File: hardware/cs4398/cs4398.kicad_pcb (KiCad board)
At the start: 4 copper layers, 55 parts, among them J1 USB_C_Receptacle_USB2.0_16P, Q1 Si2323DS, U2 STM32H750IBKx, U3 TPS65131RGE, U4 USB3300-EZK, U5 TPS7A8300, U7 TPS60151DRV, Y1 CSTCE12M

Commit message: sync 9.15
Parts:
- removed the C13 at (133.1, 89.9)
- removed the C31 at (138.9, 93.8)
- removed the R5 at (190.7, 146.4)
- added C1: 10u, Capacitor_SMD:C_0805_2012Metric, F.Cu at (191.2, 116.2)
- added C16: 100n, Capacitor_SMD:C_0402_1005Metric, B.Cu at (195.4, 108.0)
- added C18: 100n, Capacitor_SMD:C_0402_1005Metric, B.Cu at (192.2, 108.0)
- added C19: 100u, Capacitor_Tantalum_SMD:CP_EIA-3528-15_AVX-H, F.Cu at (198.2, 105.2)
- added C20: 10u, Capacitor_SMD:C_0805_2012Metric, F.Cu at (191.0, 105.8)
- added C21: 100n, Capacitor_SMD:C_0402_1005Metric, B.Cu at (196.8, 108.0)
- added C22: 4.7u, Capacitor_SMD:C_0805_2012Metric, B.Cu at (202.8, 148.8)
- added C23: 33u, Capacitor_Tantalum_SMD:CP_EIA-3528-15_AVX-H, F.Cu at (199.6, 111.0)
- added C35: 100n, Capacitor_SMD:C_0603_1608Metric, F.Cu at (193.6, 144.1)
- added C4: 33u, Capacitor_Tantalum_SMD:CP_EIA-3528-15_AVX-H, F.Cu at (198.2, 116.7)
- added C41: 100n, Capacitor_SMD:C_0603_1608Metric, B.Cu at (181.0, 131.6)
- added C44: 6800p, Capacitor_SMD:C_0402_1005Metric, F.Cu at (144.8, 143.3)
- added C45: 6800p, Capacitor_SMD:C_0402_1005Metric, F.Cu at (147.6, 137.3)
- added C46: 100n, Capacitor_SMD:C_0402_1005Metric, B.Cu at (194.2, 123.3)
- added C47: 100n, Capacitor_SMD:C_0402_1005Metric, B.Cu at (192.2, 123.8)
- added C48: 18n, Capacitor_SMD:C_0402_1005Metric, F.Cu at (144.8, 137.3)
- added C49: 18n, Capacitor_SMD:C_0402_1005Metric, F.Cu at (147.6, 139.3)
- added C51: 100n, Capacitor_SMD:C_0402_1005Metric, B.Cu at (196.4, 123.8)
- added C52: 100n, Capacitor_SMD:C_0402_1005Metric, B.Cu at (192.6, 126.1)
- added C53: 100u, Capacitor_Tantalum_SMD:CP_EIA-3528-15_AVX-H, F.Cu at (137.5, 131.3)
- added C54: 100u, Capacitor_Tantalum_SMD:CP_EIA-3528-15_AVX-H, F.Cu at (131.1, 144.9)
- added C55: 100n, Capacitor_SMD:C_0402_1005Metric, B.Cu at (192.6, 127.2)
- added C56: 100n, Capacitor_SMD:C_0402_1005Metric, B.Cu at (199.3, 126.5)
- added C57: 4700p, Capacitor_SMD:C_0402_1005Metric, F.Cu at (147.6, 135.4)
- added C58: 4700p, Capacitor_SMD:C_0402_1005Metric, F.Cu at (147.6, 141.3)
- added C59: 100n, Capacitor_SMD:C_0402_1005Metric, B.Cu at (199.3, 127.6)
- added C6: 100n, Capacitor_SMD:C_0402_1005Metric, B.Cu at (188.9, 108.0)
- added C60: 100n, Capacitor_SMD:C_0402_1005Metric, B.Cu at (199.4, 128.7)
- added C61: 100n, Capacitor_SMD:C_0603_1608Metric, B.Cu at (207.9, 129.8)
- added C62: 100n, Capacitor_SMD:C_0603_1608Metric, F.Cu at (136.4, 143.7)
- added C62: 1800p, Capacitor_SMD:C_0805_2012Metric, F.Cu at (132.2, 128.0)
- added C63: 1800p, Capacitor_SMD:C_0805_2012Metric, F.Cu at (132.2, 137.0)
- added C64: 100n, Capacitor_SMD:C_0402_1005Metric, B.Cu at (195.3, 123.3)
- added C65: 100n, Capacitor_SMD:C_0402_1005Metric, B.Cu at (191.2, 128.9)
- added C66: 100n, Capacitor_SMD:C_0402_1005Metric, B.Cu at (193.2, 123.3)
- added C67: 100n, Capacitor_SMD:C_0402_1005Metric, B.Cu at (196.7, 132.0)
- added C68: 100n, Capacitor_SMD:C_0402_1005Metric, F.Cu at (144.8, 139.3)
- added C69: 22u, Capacitor_Tantalum_SMD:CP_EIA-3528-15_AVX-H, F.Cu at (137.5, 135.7)
- added C7: 100n, Capacitor_SMD:C_0402_1005Metric, B.Cu at (196.8, 113.9)
- added C70: 22u, Capacitor_Tantalum_SMD:CP_EIA-3528-15_AVX-H, F.Cu at (131.1, 140.6)
- added C71: 100n, Capacitor_SMD:C_0402_1005Metric, B.Cu at (189.3, 131.3)
- added C72: 100n, Capacitor_SMD:C_0402_1005Metric, B.Cu at (189.3, 132.3)
- added C73: 100u, Capacitor_SMD:C_0805_2012Metric, F.Cu at (132.2, 131.0)
- added C73: 100n, Capacitor_SMD:C_0402_1005Metric, B.Cu at (194.5, 132.0)
- added C74: 100n, Capacitor_SMD:C_0402_1005Metric, B.Cu at (195.6, 132.0)
- added C75: 22u, Capacitor_SMD:C_0805_2012Metric, F.Cu at (132.2, 134.0)
- added C75: 100n, Capacitor_SMD:C_0603_1608Metric, B.Cu at (207.9, 124.2)
- added C76: 100n, Capacitor_SMD:C_0603_1608Metric, B.Cu at (180.9, 122.4)
- added C77: 100n, Capacitor_SMD:C_0402_1005Metric, B.Cu at (191.1, 123.8)
- added C78: 100n, Capacitor_SMD:C_0402_1005Metric, B.Cu at (197.9, 129.4)
- added C79: 100n, Capacitor_SMD:C_0402_1005Metric, F.Cu at (144.8, 141.3)
- added C8: 100n, Capacitor_SMD:C_0402_1005Metric, B.Cu at (192.2, 113.9)
- added C80: 2.2u, Capacitor_SMD:C_0402_1005Metric, B.Cu at (198.1, 125.0)
- added C81: 2.2u, Capacitor_SMD:C_0402_1005Metric, B.Cu at (196.8, 129.7)
- added F1: 1A, Fuse:Fuse_0603_1608Metric, B.Cu at (207.2, 109.7)
- added J2: GH1.25-4P, Connector_JST:JST_GH_BM04B-GHS-TBT_1x04-1MP_P1.25mm_Vertical, F.Cu at (207.7, 111.6)
- added Q2: S9012, Package_TO_SOT_SMD:SOT-23, F.Cu at (127.5, 122.9)
- added Q3: S9012, Package_TO_SOT_SMD:SOT-23, F.Cu at (127.5, 127.5)
- added Q4: S9013, Package_TO_SOT_SMD:SOT-23, F.Cu at (127.5, 132.1)
- added Q5: S9013, Package_TO_SOT_SMD:SOT-23, F.Cu at (127.5, 136.7)
- added R1: 10K, Resistor_SMD:R_0402_1005Metric, B.Cu at (195.7, 113.9)
- added R10: 2k, Resistor_SMD:R_0402_1005Metric, F.Cu at (150.6, 123.4)
- added R12: 10K, Resistor_SMD:R_0402_1005Metric, F.Cu at (150.6, 125.4)
- added R13: 10K, Resistor_SMD:R_0402_1005Metric, F.Cu at (147.7, 129.4)
- added R13: 10k, Resistor_SMD:R_0603_1608Metric, F.Cu at (136.4, 146.2)
- added R14: 10K, Resistor_SMD:R_0402_1005Metric, F.Cu at (150.6, 127.4)
- added R15: 1.5K, Resistor_SMD:R_0402_1005Metric, F.Cu at (147.7, 131.4)
- added R16: 1.5K, Resistor_SMD:R_0402_1005Metric, F.Cu at (150.6, 129.4)
- added R20: 10k, Resistor_SMD:R_0603_1608Metric, F.Cu at (195.2, 144.1)
- added R22: 10k, Resistor_SMD:R_0603_1608Metric, B.Cu at (181.0, 129.8)
- added R23: 1.6k, Resistor_SMD:R_0402_1005Metric, F.Cu at (141.9, 121.5)
- added R24: 620, Resistor_SMD:R_0402_1005Metric, F.Cu at (141.9, 127.4)
- added R25: 1.6k, Resistor_SMD:R_0402_1005Metric, F.Cu at (144.8, 123.4)
- added R26: 620, Resistor_SMD:R_0402_1005Metric, F.Cu at (144.8, 125.4)
- added R27: 270, Resistor_SMD:R_0402_1005Metric, F.Cu at (141.9, 129.4)
- added R28: 270, Resistor_SMD:R_0402_1005Metric, F.Cu at (144.8, 127.4)
- added R29: 680, Resistor_SMD:R_0402_1005Metric, F.Cu at (141.9, 123.4)
- added R30: 270, Resistor_SMD:R_0402_1005Metric, F.Cu at (141.9, 125.4)
- added R31: 680, Resistor_SMD:R_0402_1005Metric, F.Cu at (144.8, 129.4)
- added R32: 270, Resistor_SMD:R_0402_1005Metric, F.Cu at (144.8, 131.4)
- added R33: 100, Resistor_SMD:R_0603_1608Metric, B.Cu at (207.2, 113.4)
- added R34: 100, Resistor_SMD:R_0603_1608Metric, B.Cu at (207.2, 111.6)
- added R35: 1.2k, Resistor_SMD:R_0402_1005Metric, F.Cu at (141.9, 131.4)
- added R36: 1.2k, Resistor_SMD:R_0402_1005Metric, F.Cu at (144.8, 133.4)
- added R37: 10k, Resistor_SMD:R_0603_1608Metric, B.Cu at (207.9, 131.7)
- added R38: 4.7K, Resistor_SMD:R_0603_1608Metric, B.Cu at (204.6, 114.2)
- added R39: 4.7K, Resistor_SMD:R_0603_1608Metric, B.Cu at (204.6, 110.8)
- added R40: 100k, Resistor_SMD:R_0402_1005Metric, F.Cu at (141.9, 133.4)
- added R41: 100k, Resistor_SMD:R_0402_1005Metric, F.Cu at (147.7, 121.5)
- added R42: 560, Resistor_SMD:R_0402_1005Metric, F.Cu at (144.8, 121.5)
- added R43: 560, Resistor_SMD:R_0402_1005Metric, F.Cu at (147.7, 123.4)
- added R44: 10k, Resistor_SMD:R_0603_1608Metric, B.Cu at (207.9, 122.3)
- added R45: 10k, Resistor_SMD:R_0603_1608Metric, B.Cu at (181.0, 124.2)
- added R46: 10k, Resistor_SMD:R_0402_1005Metric, B.Cu at (194.6, 125.7)
- added R7: 5.1k, Resistor_SMD:R_0402_1005Metric, F.Cu at (147.7, 127.4)
- added R8: 5.1k, Resistor_SMD:R_0402_1005Metric, F.Cu at (150.6, 121.5)
- added R9: 2k, Resistor_SMD:R_0402_1005Metric, F.Cu at (147.7, 125.4)
- added SW1: SW_Omron_B3FS, Button_Switch_SMD:SW_SPST_TS-1088-xR025, F.Cu at (181.0, 130.7)
- added SW2: SW_Omron_B3FS, Button_Switch_SMD:SW_SPST_TS-1088-xR025, F.Cu at (207.9, 130.7)
- added SW3: SW_Omron_B3FS, Button_Switch_SMD:SW_SPST_TS-1088-xR025, F.Cu at (207.9, 123.3)
- added SW4: SW_Omron_B3FS, Button_Switch_SMD:SW_SPST_TS-1088-xR025, F.Cu at (181.0, 123.3)
- added U3: CS4398, Package_SO:TSSOP-28_4.4x9.7mm_P0.65mm, F.Cu at (192.5, 111.0)
- added U6: OPA1612AxD, Package_SON:WSON-8-1EP_3x3mm_P0.5mm_EP1.2x2mm_ThermalVias, F.Cu at (137.5, 140.1)
- added Y2: CSTCE24M, Crystal:Resonator_SMD_Murata_CSTxExxV-3Pin_3.0x1.1mm, F.Cu at (187.2, 127.0)
- R11: value 1.5k -> 10K
- Y1: value CSTCE12M -> CSTCE24M
- moved U7 59.6 mm to (194.6, 127.3)
- moved R11 27.8 mm to (147.7, 133.4)
- renumbered C22 to C11, C11 to C12, C28 to C13, C21 to C14, C23 to C15, C24 to C17, C4 to C2, C7 to C24, C6 to C25, C12 to C26, C5 to C27, C14 to C28, C2 to C29, C9 to C3, C20 to C30, C19 to C31, C25 to C32, C17 to C33, C1 to C34, C42 to C36, C16 to C37, C29 to C38, C15 to C39, C18 to C40, C26 to C42, C30 to C43, C8 to C5, C27 to C50, C3 to C9, R9 to R17, R10 to R18, R7 to R19, R1 to R2, R8 to R21, R2 to R3, R6 to R4, R4 to R5, R3 to R6, U7 to U1, U5 to U2, U3 to U4, U4 to U5, U2 to U7
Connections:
- R11 pad 1: Net-(U5-PG) -> +5V
- R11 pad 2: +3.3V -> Net-(Q2-B)
- U5 pad 11: unconnected-(U4-NXT-Pad11) -> /NXT
- U5 pad 12: unconnected-(U4-DIR-Pad12) -> /DIR
- U5 pad 13: unconnected-(U4-STP-Pad13) -> /STP
- U5 pad 14: unconnected-(U4-CLKOUT-Pad14) -> /CK
- U5 pad 17: unconnected-(U4-DATA7-Pad17) -> /D7
- U5 pad 18: unconnected-(U4-DATA6-Pad18) -> /D6
- U5 pad 19: unconnected-(U4-DATA5-Pad19) -> /D5
- U5 pad 20: unconnected-(U4-DATA4-Pad20) -> /D4
- U5 pad 21: unconnected-(U4-DATA3-Pad21) -> /D3
- U5 pad 22: unconnected-(U4-DATA2-Pad22) -> /D2
- U5 pad 23: unconnected-(U4-DATA1-Pad23) -> /D1
- U5 pad 24: unconnected-(U4-DATA0-Pad24) -> /D0
- U5 pad 9: unconnected-(U4-RESET-Pad9) -> /USB_RS
- U7 pad A10: unconnected-(U2-PB3-PadA10) -> /SCLK
- U7 pad A11: unconnected-(U2-PD7-PadA11) -> /SDATA
- U7 pad A13: unconnected-(U2-PA15-PadA13) -> /LRCK
- U7 pad A14: unconnected-(U2-PA14-PadA14) -> /CLK
- U7 pad A15: unconnected-(U2-PA13-PadA15) -> /DIO
- U7 pad A6: unconnected-(U2-PB5-PadA6) -> /D7
- U7 pad C6: unconnected-(U2-PDR_ON-PadC6) -> +3.3V
- U7 pad D1: unconnected-(U2-PC13-PadD1) -> /SW2
- U7 pad D6: unconnected-(U2-BOOT0-PadD6) -> Net-(U7-BOOT0)
- U7 pad E4: unconnected-(U2-PI11-PadE4) -> /DIR
- U7 pad F13: unconnected-(U2-VCAP-PadF13) -> Net-(C80-Pad1)
- U7 pad F15: unconnected-(U2-PA8-PadF15) -> /SW3
- U7 pad G1: unconnected-(U2-PH0-PadG1) -> Net-(U7-PH0)
- U7 pad H1: unconnected-(U2-PH1-PadH1) -> Net-(U7-PH1)
- U7 pad H4: unconnected-(U2-PH4-PadH4) -> /NXT
- U7 pad J1: unconnected-(U2-NRST-PadJ1) -> /RS
- U7 pad M10: unconnected-(U2-VCAP-PadM10) -> Net-(C81-Pad1)
- U7 pad M2: unconnected-(U2-PC0-PadM2) -> /STP
- U7 pad N1: unconnected-(U2-VREF--PadN1) -> GND
- U7 pad N15: unconnected-(U2-PD10-PadN15) -> /SW1
- U7 pad N5: unconnected-(U2-PC4-PadN5) -> /MCLK
- U7 pad P1: unconnected-(U2-VREF+-PadP1) -> +3.3V
- U7 pad P12: unconnected-(U2-PB12-PadP12) -> /D5
- U7 pad P13: unconnected-(U2-PB13-PadP13) -> /D6
- U7 pad P15: unconnected-(U2-PD8-PadP15) -> /USB_RS
- U7 pad P4: unconnected-(U2-PA5-PadP4) -> /CK
- U7 pad R12: unconnected-(U2-PB10-PadR12) -> /D3
- U7 pad R13: unconnected-(U2-PB11-PadR13) -> /D4
- U7 pad R2: unconnected-(U2-PA3-PadR2) -> /D0
- U7 pad R4: unconnected-(U2-PB1-PadR4) -> /D2
- U7 pad R5: unconnected-(U2-PB0-PadR5) -> /D1
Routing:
- net +3.3V: track 24.0 -> 228.5 mm, vias 6 -> 44
- net +5V: track 1.29 -> 65.4 mm, vias 0 -> 13
- net GND: track 30.9 -> 72.9 mm, vias 80 -> 166
- net -15V: track 11.8 -> 44.0 mm
- net /D7: track 0.00 -> 28.6 mm, vias 0 -> 1
- net /MCLK: track 0.00 -> 23.0 mm, vias 0 -> 4
- net /USB_RS: track 0.00 -> 21.0 mm, vias 0 -> 2
- net /DIR: track 0.00 -> 19.9 mm, vias 0 -> 2
- net /CLK: track 0.00 -> 17.6 mm, vias 0 -> 1
- net /NXT: track 0.00 -> 15.9 mm, vias 0 -> 2
- net /SDATA: track 0.00 -> 15.8 mm, vias 0 -> 4
- net /DIO: track 0.00 -> 15.2 mm, vias 0 -> 1
- net /LRCK: track 0.00 -> 14.9 mm, vias 0 -> 2
- net /SCLK: track 0.00 -> 14.4 mm, vias 0 -> 2
- net /D5: track 0.00 -> 14.0 mm, vias 0 -> 2
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- added copper zone on B.Cu, net +5V
- added copper zone on F.Cu, net +5V
- added copper zone on In2.Cu, net +5V

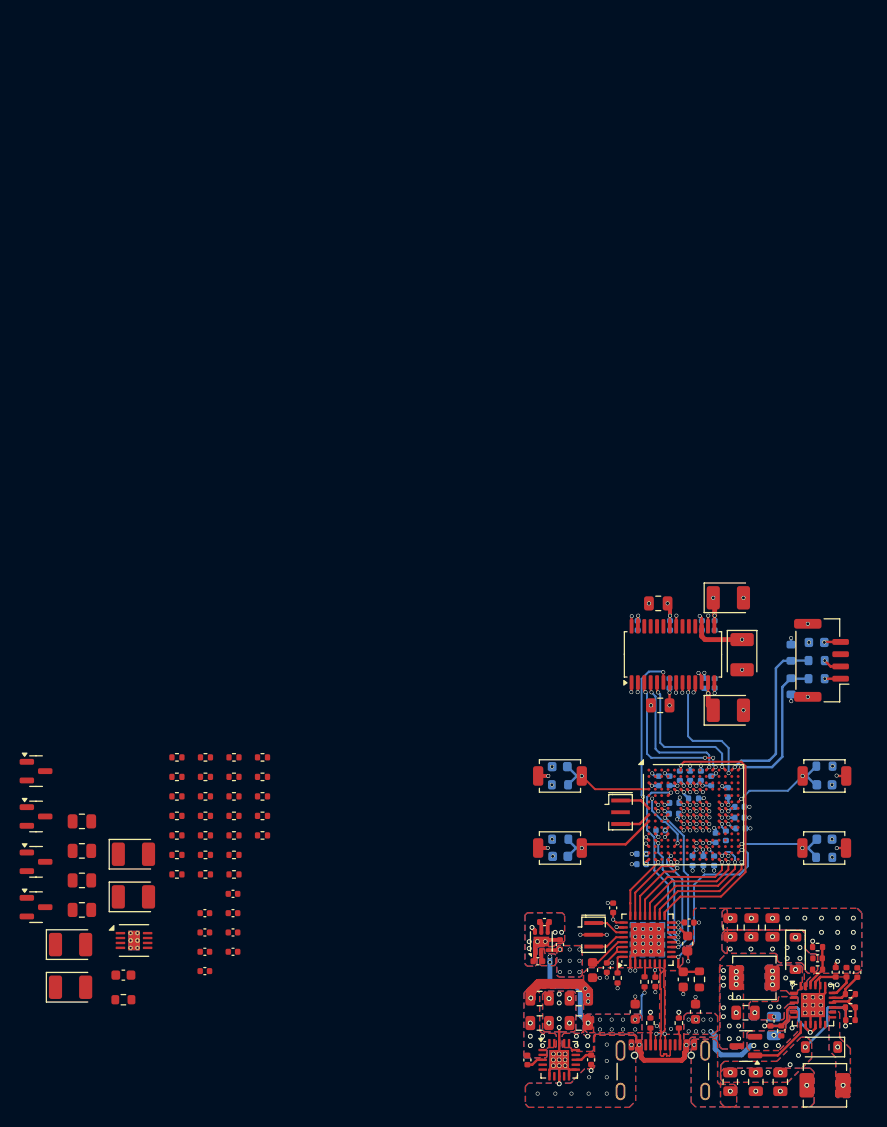
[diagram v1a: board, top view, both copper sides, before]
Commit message: 添加4.4mm平衡输出
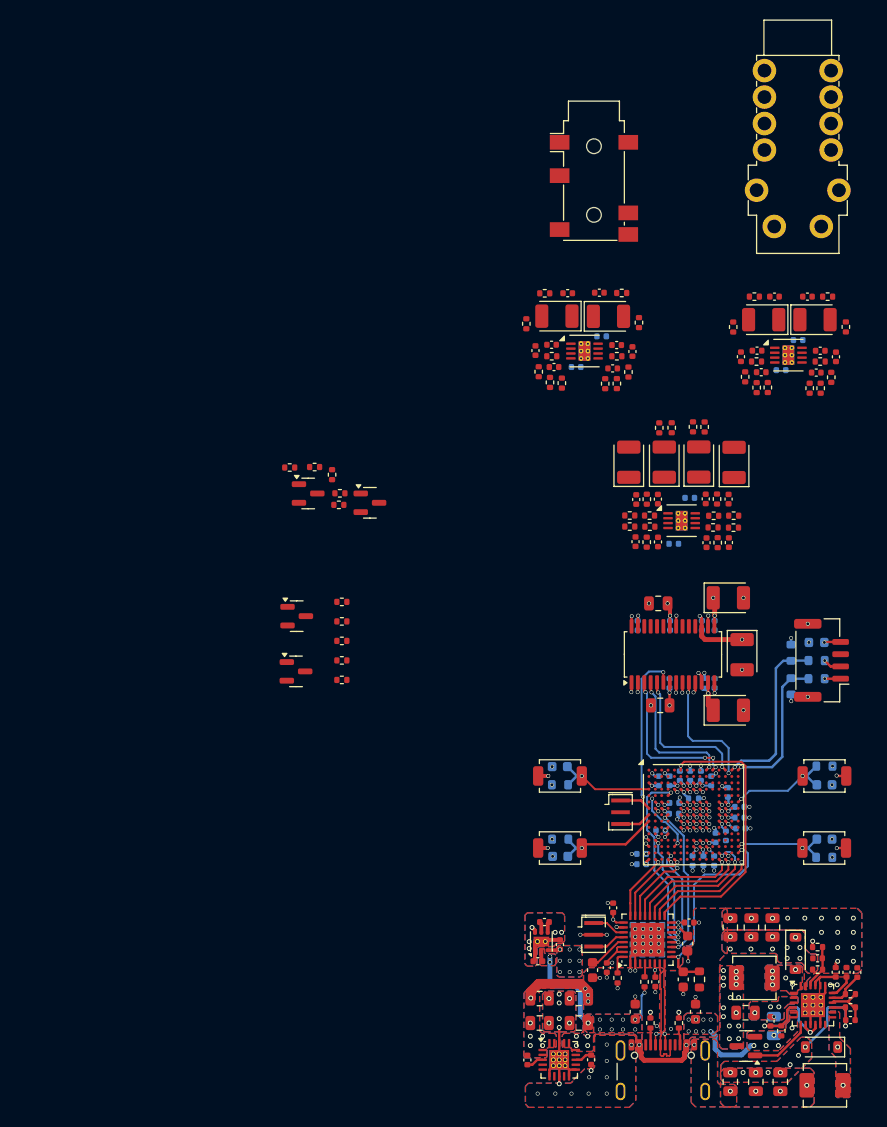
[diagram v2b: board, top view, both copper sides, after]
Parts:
- removed the C73 at (132.2, 131.0)
- removed the C75 at (132.2, 134.0)
- added C1: 15n, Capacitor_SMD:C_0402_1005Metric, F.Cu at (186.3, 81.8)
- added C13: 18n, Capacitor_SMD:C_0402_1005Metric, F.Cu at (186.8, 79.4)
- added C14: 18n, Capacitor_SMD:C_0402_1005Metric, F.Cu at (180.1, 79.4)
- added C2: 15n, Capacitor_SMD:C_0402_1005Metric, F.Cu at (180.4, 81.6)
- added C21: 47u, Capacitor_Tantalum_SMD:CP_EIA-3528-15_AVX-H, F.Cu at (185.9, 76.5)
- added C22: 47u, Capacitor_Tantalum_SMD:CP_EIA-3528-15_AVX-H, F.Cu at (180.7, 76.5)
- added C26: 6800p, Capacitor_SMD:C_0402_1005Metric, F.Cu at (185.0, 74.1)
- added C27: 6800p, Capacitor_SMD:C_0402_1005Metric, F.Cu at (181.8, 74.1)
- added C35: 100n, Capacitor_SMD:C_0402_1005Metric, B.Cu at (185.2, 78.5)
- added C4: 2200p, Capacitor_SMD:C_0402_1005Metric, F.Cu at (188.4, 80.1)
- added C41: 100n, Capacitor_SMD:C_0402_1005Metric, B.Cu at (182.6, 81.6)
- added C42: 15n, Capacitor_SMD:C_0402_1005Metric, F.Cu at (207.1, 82.2)
- added C43: 15n, Capacitor_SMD:C_0402_1005Metric, F.Cu at (201.5, 82.2)
- added C44: 2200p, Capacitor_SMD:C_0402_1005Metric, F.Cu at (209.1, 80.6)
- added C45: 2200p, Capacitor_SMD:C_0402_1005Metric, F.Cu at (199.4, 80.6)
- added C5: 2200p, Capacitor_SMD:C_0402_1005Metric, F.Cu at (178.5, 80.0)
- added C50: 100n, Capacitor_SMD:C_0402_1005Metric, B.Cu at (205.3, 78.9)
- added C51: 18n, Capacitor_SMD:C_0402_1005Metric, F.Cu at (207.5, 80.0)
- added C52: 18n, Capacitor_SMD:C_0402_1005Metric, F.Cu at (201.1, 80.0)
- added C61: 47u, Capacitor_Tantalum_SMD:CP_EIA-3528-15_AVX-H, F.Cu at (207.0, 76.8)
- added C63: 100n, Capacitor_SMD:C_0402_1005Metric, B.Cu at (203.5, 82.0)
- added C77: 6800p, Capacitor_SMD:C_0402_1005Metric, F.Cu at (206.2, 74.5)
- added C78: 6800p, Capacitor_SMD:C_0402_1005Metric, F.Cu at (202.9, 74.5)
- added J1: AudioJack3_Ground_SwitchTR, Connector_Audio:Jack_3.5mm_PJ311_Horizontal, F.Cu at (184.4, 63.4)
- added J3: AudioJack3_Ground_Switch, Connector_Audio:Jack_6.35mm_Neutrik_NSJ12HH-1_Horizontal, F.Cu at (208.6, 51.4)
- added R1: 100K, Resistor_SMD:R_0402_1005Metric, F.Cu at (185.6, 83.3)
- added R12: 100k, Resistor_SMD:R_0402_1005Metric, F.Cu at (189.0, 77.1)
- added R14: 330, Resistor_SMD:R_0402_1005Metric, F.Cu at (187.3, 74.1)
- added R15: 330, Resistor_SMD:R_0402_1005Metric, F.Cu at (179.4, 74.1)
- added R18: 100K, Resistor_SMD:R_0402_1005Metric, F.Cu at (206.4, 83.8)
- added R19: 100K, Resistor_SMD:R_0402_1005Metric, F.Cu at (202.2, 83.7)
- added R2: 100K, Resistor_SMD:R_0402_1005Metric, F.Cu at (181.2, 83.3)
- added R23: 200, Resistor_SMD:R_0402_1005Metric, F.Cu at (207.6, 83.8)
- added R24: 200, Resistor_SMD:R_0402_1005Metric, F.Cu at (201.0, 83.7)
- added R29: 680, Resistor_SMD:R_0402_1005Metric, F.Cu at (199.9, 82.6)
- added R3: 200, Resistor_SMD:R_0402_1005Metric, F.Cu at (186.8, 83.3)
- added R30: 680, Resistor_SMD:R_0402_1005Metric, F.Cu at (208.6, 82.7)
- added R34: 470, Resistor_SMD:R_0402_1005Metric, F.Cu at (207.5, 81.1)
- added R35: 470, Resistor_SMD:R_0402_1005Metric, F.Cu at (201.0, 81.1)
- added R4: 200, Resistor_SMD:R_0402_1005Metric, F.Cu at (180.0, 83.2)
- added R45: 100k, Resistor_SMD:R_0402_1005Metric, F.Cu at (210.1, 77.5)
- added R46: 100k, Resistor_SMD:R_0402_1005Metric, F.Cu at (198.6, 77.6)
- added R49: 330, Resistor_SMD:R_0402_1005Metric, F.Cu at (208.3, 74.5)
- added R5: 680, Resistor_SMD:R_0402_1005Metric, F.Cu at (178.8, 82.1)
- added R50: 330, Resistor_SMD:R_0402_1005Metric, F.Cu at (200.8, 74.5)
- added R6: 680, Resistor_SMD:R_0402_1005Metric, F.Cu at (188.0, 82.2)
- added R8: 470, Resistor_SMD:R_0402_1005Metric, F.Cu at (186.8, 80.5)
- added R9: 470, Resistor_SMD:R_0402_1005Metric, F.Cu at (180.1, 80.5)
- added U3: OPA1612AxD, Package_SON:WSON-8-1EP_3x3mm_P0.5mm_EP1.2x2mm_ThermalVias, F.Cu at (183.5, 80.0)
- added U7: OPA1612AxD, Package_SON:WSON-8-1EP_3x3mm_P0.5mm_EP1.2x2mm_ThermalVias, F.Cu at (204.3, 80.4)
- C103: renamed from C79; moved to B.Cu
- C62: value 100n -> 47u; footprint Capacitor_SMD:C_0603_1608Metric -> Capacitor_Tantalum_SMD:CP_EIA-3528-15_AVX-H
- C86: renamed from C62; footprint Capacitor_SMD:C_0805_2012Metric -> Capacitor_SMD:C_0402_1005Metric
- C87: renamed from C63; footprint Capacitor_SMD:C_0805_2012Metric -> Capacitor_SMD:C_0402_1005Metric
- C92: renamed from C68; moved to B.Cu
- R13: value 10k -> 100k; footprint Resistor_SMD:R_0603_1608Metric -> Resistor_SMD:R_0402_1005Metric
- moved C62 93.5 mm to (201.8, 76.8), turned to 180 degrees
- moved C76 86.3 mm to (198.7, 91.4), turned to 90 degrees
- moved C94 80.8 mm to (195.1, 91.3), turned to 90 degrees
- moved R13 80.3 mm to (177.5, 77.2), turned to -90 degrees
- moved C87 73.9 mm to (195.9, 99.6), turned to -90 degrees
- moved U8 70.4 mm to (193.4, 97.3)
- moved C93 70.0 mm to (191.6, 91.3), turned to 90 degrees
- moved C71 67.1 mm to (198.2, 95.1), turned to 90 degrees
- moved R64 67.0 mm to (191.1, 87.8), turned to 90 degrees
- moved C82 66.8 mm to (195.8, 95.1), turned to 90 degrees
- moved C92 66.4 mm to (194.2, 95.0)
- moved C86 65.3 mm to (191.0, 99.5), turned to 90 degrees
- moved C75 64.4 mm to (188.0, 91.3), turned to 90 degrees
- moved C103 63.4 mm to (192.6, 99.7), turned to 180 degrees
- moved C67 63.1 mm to (198.2, 99.5), turned to -90 degrees
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- renumbered C6 to C10, C76 to C100, C77 to C101, C78 to C102, C80 to C104, C81 to C105, C7 to C11, C8 to C12, C9 to C15, C10 to C16, C11 to C17, C12 to C18, C13 to C19, C14 to C20, C15 to C23, C16 to C24, C17 to C25, C18 to C28, C19 to C29, C1 to C3, C20 to C30, C21 to C31, C22 to C32, C23 to C33, C24 to C34, C25 to C36, C26 to C37, C27 to C38, C28 to C39, C29 to C40, C30 to C46, C31 to C47, C32 to C48, C33 to C49, C34 to C53, C35 to C54, C36 to C55, C37 to C56, C38 to C57, C39 to C58, C40 to C59, C2 to C6, C41 to C60, C42 to C64, C43 to C65, C44 to C66, C45 to C67, C46 to C68, C47 to C69, C3 to C7, C48 to C70, C49 to C71, C50 to C72, C51 to C73, C52 to C74, C53 to C75, C54 to C76, C55 to C79, C4 to C8, C56 to C80, C57 to C81, C58 to C82, C59 to C83, C60 to C84, C61 to C85, C64 to C88, C65 to C89, C5 to C9, C66 to C90, C67 to C91, C69 to C93, C70 to C94, C71 to C95, C72 to C96, C73 to C97, C74 to C98, C75 to C99, J1 to J2, J2 to J4, R2 to R10, R3 to R11, R4 to R16, R5 to R17, R6 to R20, R7 to R21, R8 to R22, R9 to R25, R10 to R26, R11 to R27, R12 to R28, R13 to R31, R14 to R32, R15 to R33, R16 to R36, R17 to R37, R18 to R38, R19 to R39, R20 to R40, R21 to R41, R22 to R42, R23 to R43, R24 to R44, R25 to R47, R26 to R48, R27 to R51, R28 to R52, R29 to R53, R30 to R54, R31 to R55, R32 to R56, R33 to R57, R34 to R58, R35 to R59, R36 to R60, R37 to R61, R38 to R62, R39 to R63, R40 to R64, R41 to R65, R42 to R66, R43 to R67, R44 to R68, R45 to R69, R1 to R7, R46 to R70, U3 to U4, U4 to U5, U5 to U6, U6 to U8, U7 to U9
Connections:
- C62 pad 1: GND -> Net-(U7A--)
- C62 pad 2: /RS3 -> Net-(C62-Pad2)
- R13 pad 1: /RS3 -> GND
- R13 pad 2: +3V3 -> Net-(C22-Pad2)
